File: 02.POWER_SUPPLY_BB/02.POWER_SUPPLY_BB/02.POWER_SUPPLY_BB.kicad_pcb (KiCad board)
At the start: 2 copper layers, 17 parts, among them J1 Conn_01x02_Pin, J2 Conn_01x02_Pin, J3 Conn_01x03_Pin, J4 Conn_01x03_Pin, J5 Screw_Terminal_01x02, J6 Barrel_Jack_Switch, J7 Screw_Terminal_01x02, U1 LM7806_TO220, U2 LM317_TO-220

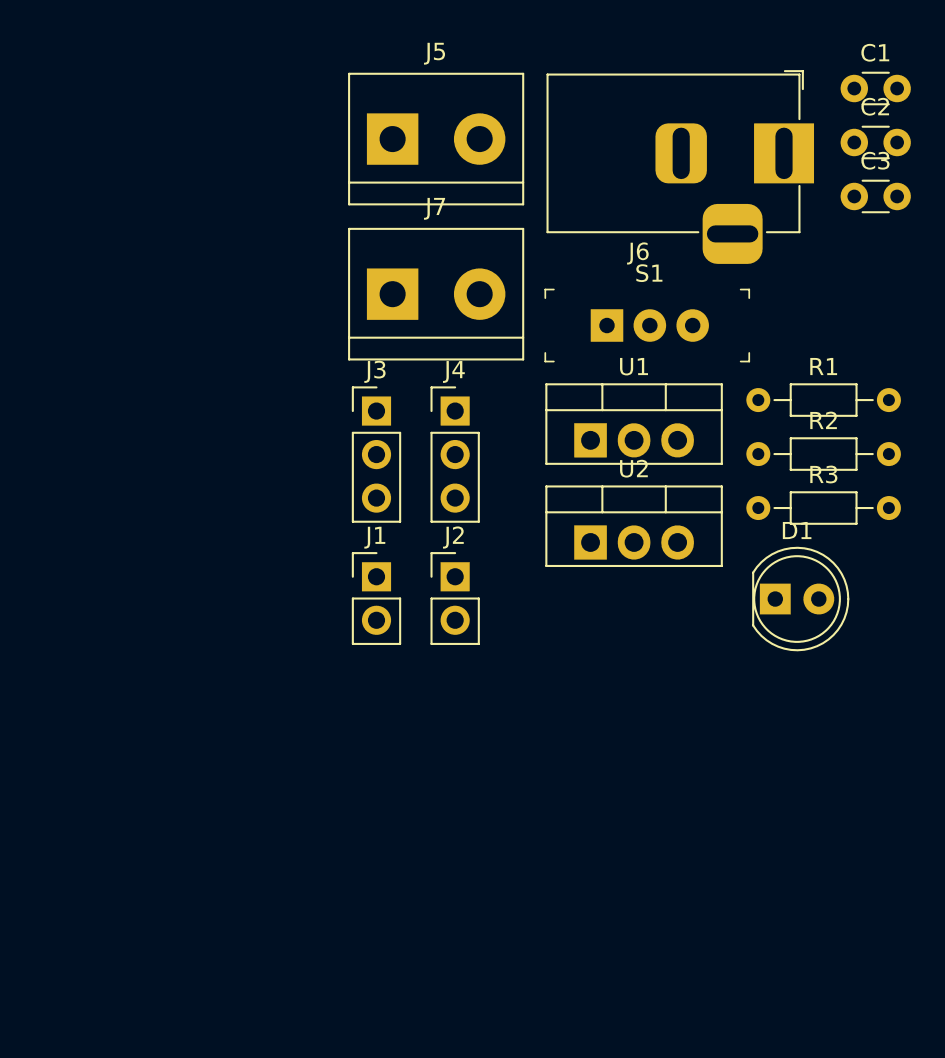
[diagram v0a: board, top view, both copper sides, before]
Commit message: POWER_SUPPLY_BB - PCB - OUTLINE AND CONSTRAINTS, FOOTPRINTS
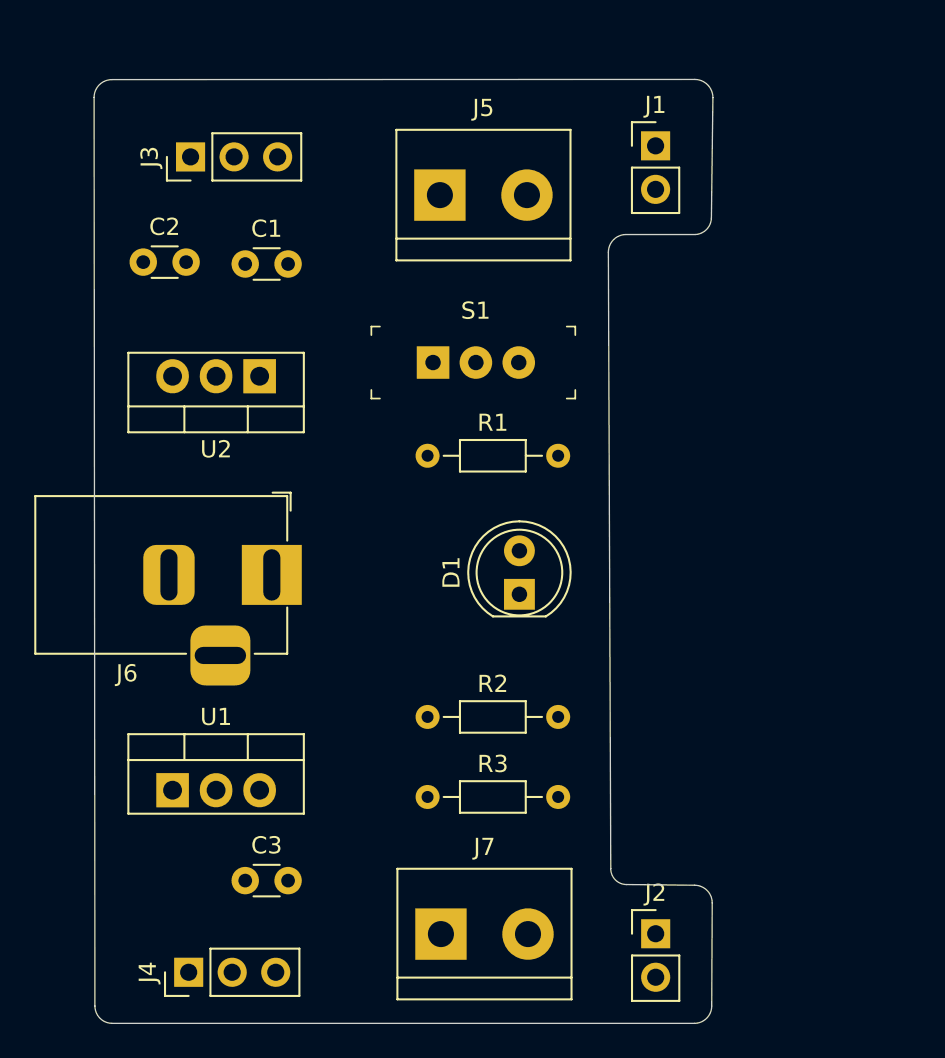
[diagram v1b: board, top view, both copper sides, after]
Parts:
- moved C3 53.4 mm to (125.8, 137.7)
- moved C2 42.1 mm to (119.8, 101.6)
- moved J6 38.7 mm to (127.3, 119.8)
- moved J7 37.4 mm to (137.2, 140.8)
- moved C1 37.0 mm to (125.8, 101.7)
- moved J4 36.3 mm to (122.5, 143.0), turned to 90 degrees
- moved U1 31.8 mm to (121.5, 132.4)
- moved J1 30.0 mm to (149.7, 94.8)
- moved R3 25.6 mm to (136.4, 132.8)
- moved R2 24.7 mm to (136.4, 128.1)
- moved J2 23.9 mm to (149.7, 140.8)
- moved U2 21.6 mm to (126.6, 108.2), turned to 180 degrees
- moved R1 19.6 mm to (136.4, 112.9)
- moved J3 18.4 mm to (122.6, 95.5), turned to 90 degrees
- moved D1 14.9 mm to (141.8, 121.0), turned to 90 degrees
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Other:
- board outline added: 36.1 x 55.1 mm
